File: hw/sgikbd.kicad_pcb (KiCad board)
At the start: 2 copper layers, 80 x 60 mm, 33 parts, among them J1 AVR-ISP, Q1 2N7002, SW1 RESET, U1 ATmega328PB, U2 ps2kbd, U3 ps2aux, U4 LM358, U5 sgi-mdin6, U6 L7805, U7 L7905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

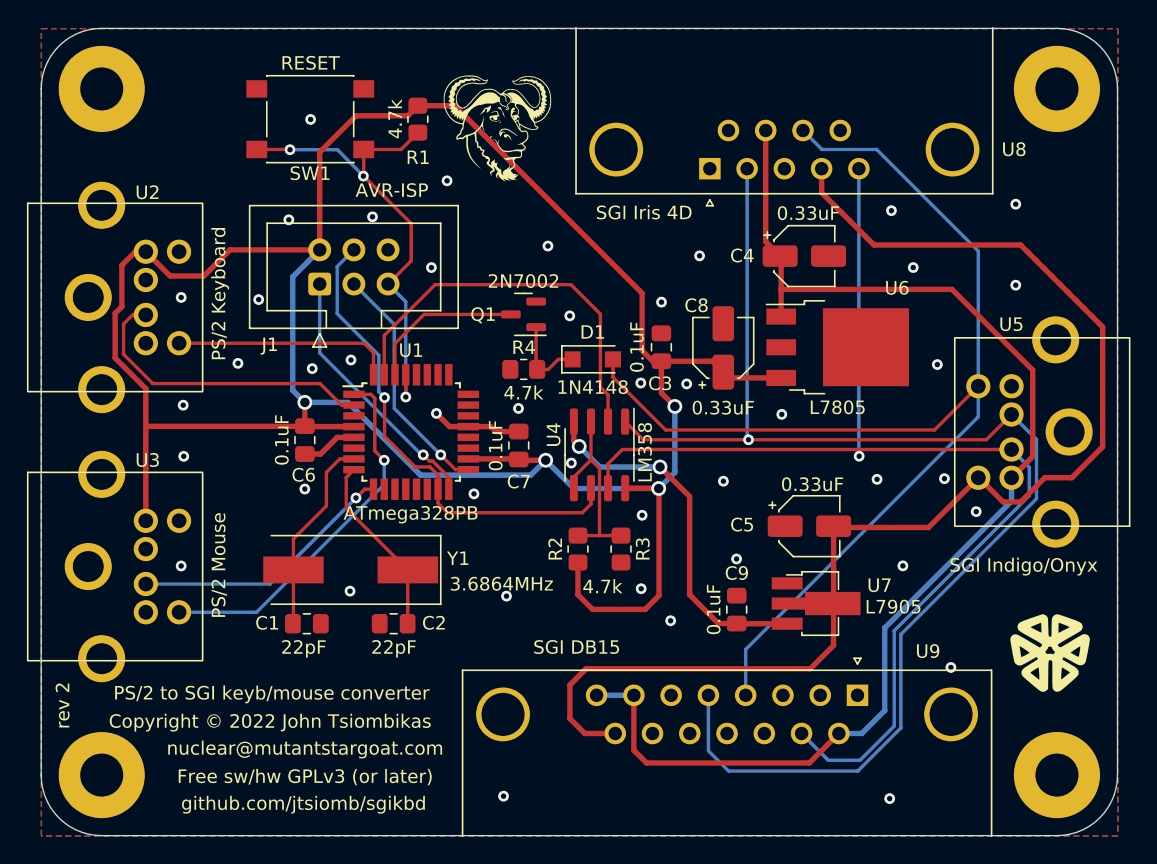
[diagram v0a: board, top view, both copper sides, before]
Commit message: rev3: jumper-selectable R3K hack
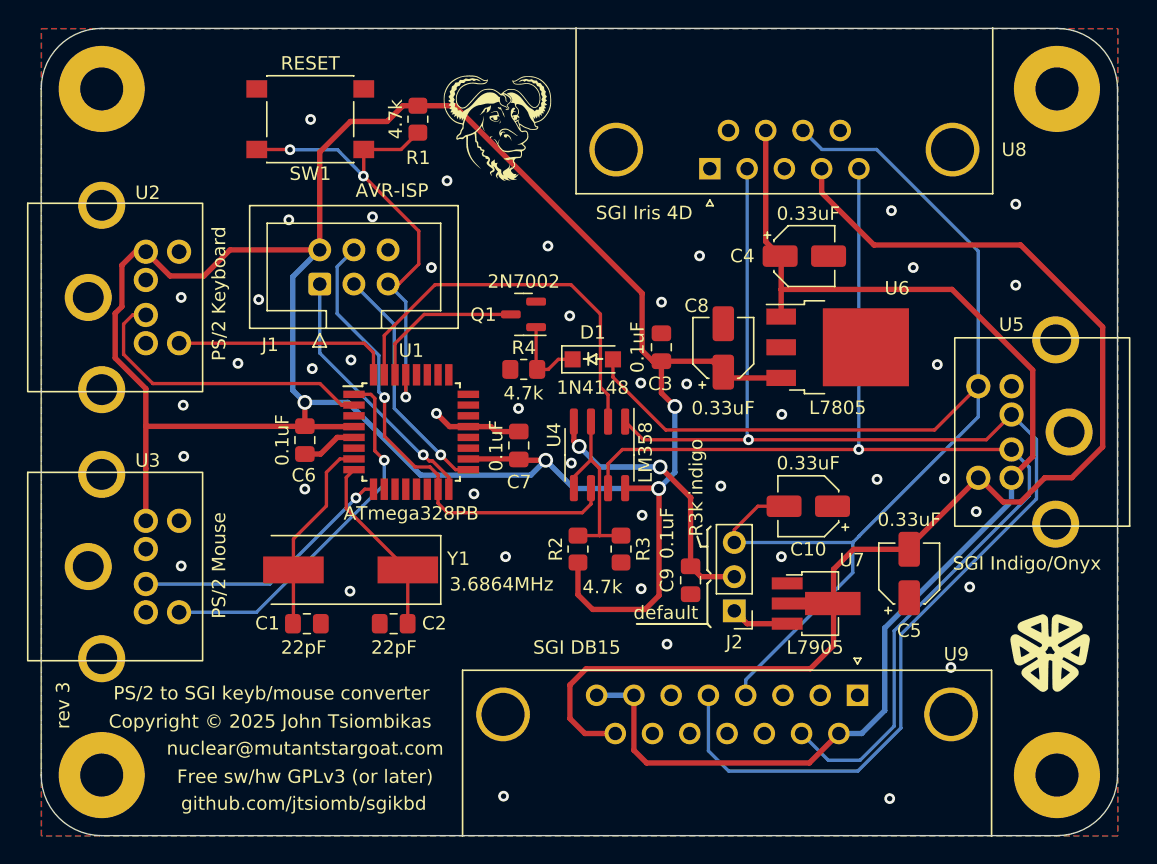
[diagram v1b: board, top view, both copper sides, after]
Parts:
- added C10: 0.33uF, Capacitor_SMD:CP_Elec_4x5.4, F.Cu at (157.0, 95.5)
- added J2: sel_no_vneg, Connector_PinHeader_2.54mm:PinHeader_1x03_P2.54mm_Vertical, F.Cu at (151.5, 103.3)
- moved C5 8.21 mm to (164.5, 100.5), turned to 90 degrees
- moved C9 4.07 mm to (148.2, 101.0), turned to 90 degrees
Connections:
- U7 pad 3: -5V -> /-5vreg
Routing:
- net /SGIKBTX: track 88.4 -> 102.5 mm
- net -5V: track 27.2 -> 20.6 mm
- net /-5vreg: track 0.00 -> 4.33 mm
- net /VBUS-: track 99.1 -> 97.3 mm
- net /~{RESET}: track 36.1 -> 37.0 mm
- net /SGIMRX: track 87.6 -> 87.1 mm
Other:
- board text added: "Copyright © 2025 John Tsiombikas"
- board text added: "J2 jumper, don't leave open 1-2: use negative voltage rail (default) 2-3: missing negative voltage rail The R3000 indigo does not provide a negative voltage rail short 2-3 to derive -5v from the keyboard Tx signal"
- board text added: "R3k indigo"
- board text added: "default"
- board text added: "rev 3"
- board text removed: "Copyright © 2022 John Tsiombikas"
- board text removed: "rev 2"
